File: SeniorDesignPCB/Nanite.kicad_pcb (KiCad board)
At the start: 2 copper layers, 20 parts, among them U1 4017, U2 TLC555

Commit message: Finished making lines?
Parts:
- moved D17 76.1 mm to (106.7, 81.3)
- moved D22 52.6 mm to (121.9, 82.5)
- moved D18 26.8 mm to (101.6, 71.1)
- moved D19 21.9 mm to (57.1, 87.6)
- moved D21 20.9 mm to (100.3, 91.4)
- moved BT1 7.73 mm to (118.1, 121.9)
- moved D20 3.59 mm to (77.5, 100.3)
- turned R2 to 90 degrees
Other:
- board outline added: 154.9 x 76.2 mm
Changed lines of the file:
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@@
   (general
     (thickness 1.6)
-    (drawings 0)
+    (drawings 5)
     (tracks 0)
     (zones 0)
@@
   )
   (module Battery:BatteryHolder_Keystone_2466_1xAAA (layer F.Cu)
-    (at 119.38 129.54)
+    (at 118.11 121.92)
     (descr "1xAAA Battery Holder, Keystone, Plastic Case, http://www.keyelco.com/product-pdf.cfm?p=1031")
     (tags "AAA battery holder Keystone")
@@
   )
   (module Diode_THT:D_DO-41_SOD81_P10.16mm_Horizontal (layer F.Cu)
-    (at 80.01 114.3)
+    (at 121.92 82.55)
     (descr "Diode, DO-41_SOD81 series, Axial, Horizontal, pin pitch=10.16mm, , length*diameter=5.2*2.7mm^2, , http://www.diodes.com/_files/packages/DO-41%20(Plastic).pdf")
     (tags "Diode DO-41_SOD81 series Axial Horizontal pin pitch 10.16mm  length 5.2mm diameter 2.7mm")
@@
   )
   (module Diode_THT:D_DO-41_SOD81_P10.16mm_Horizontal (layer F.Cu)
-    (at 80.01 96.52)
+    (at 100.33 91.44)
     (descr "Diode, DO-41_SOD81 series, Axial, Horizontal, pin pitch=10.16mm, , length*diameter=5.2*2.7mm^2, , http://www.diodes.com/_files/packages/DO-41%20(Plastic).pdf")
     (tags "Diode DO-41_SOD81 series Axial Horizontal pin pitch 10.16mm  length 5.2mm diameter 2.7mm")
@@
   )
   (module Diode_THT:D_DO-41_SOD81_P10.16mm_Horizontal (layer F.Cu)
-    (at 80.01 102.87)
+    (at 77.47 100.33)
     (descr "Diode, DO-41_SOD81 series, Axial, Horizontal, pin pitch=10.16mm, , length*diameter=5.2*2.7mm^2, , http://www.diodes.com/_files/packages/DO-41%20(Plastic).pdf")
     (tags "Diode DO-41_SOD81 series Axial Horizontal pin pitch 10.16mm  length 5.2mm diameter 2.7mm")
@@
   )
   (module Diode_THT:D_DO-41_SOD81_P10.16mm_Horizontal (layer F.Cu)
-    (at 78.74 91.44)
+    (at 57.15 87.63)
     (descr "Diode, DO-41_SOD81 series, Axial, Horizontal, pin pitch=10.16mm, , length*diameter=5.2*2.7mm^2, , http://www.diodes.com/_files/packages/DO-41%20(Plastic).pdf")
     (tags "Diode DO-41_SOD81 series Axial Horizontal pin pitch 10.16mm  length 5.2mm diameter 2.7mm")
@@
   )
   (module Diode_THT:D_DO-41_SOD81_P10.16mm_Horizontal (layer F.Cu)
-    (at 78.74 85.09)
+    (at 101.6 71.12)
     (descr "Diode, DO-41_SOD81 series, Axial, Horizontal, pin pitch=10.16mm, , length*diameter=5.2*2.7mm^2, , http://www.diodes.com/_files/packages/DO-41%20(Plastic).pdf")
     (tags "Diode DO-41_SOD81 series Axial Horizontal pin pitch 10.16mm  length 5.2mm diameter 2.7mm")
@@
   )
   (module LED_THT:LED_D5.0mm (layer F.Cu)
-    (at 43.18 123.19)
+    (at 106.68 81.28)
     (descr "LED, diameter 5.0mm, 2 pins, http://cdn-reichelt.de/documents/datenblatt/A500/LL-504BC2E-009.pdf")
     (tags "LED diameter 5.0mm 2 pins")
@@
   )
   (module Resistor_THT:R_Axial_DIN0309_L9.0mm_D3.2mm_P2.54mm_Vertical (layer F.Cu)
-    (at 91.44 132.08)
+    (at 91.44 132.08 90)
     (descr "Resistor, Axial_DIN0309 series, Axial, Vertical, pin pitch=2.54mm, 0.5W = 1/2W, length*diameter=9*3.2mm^2, http://cdn-reichelt.de/documents/datenblatt/B400/1_4W%23YAG.pdf")
     (tags "Resistor Axial_DIN0309 series Axial Vertical pin pitch 2.54mm 0.5W = 1/2W length 9mm diameter 3.2mm")
-    (fp_text reference R2 (at 1.27 -2.72) (layer F.SilkS)
-      (effects (font (size 1 1) (thickness 0.15)))
-    )
-    (fp_text value 4.7k (at 1.27 2.72) (layer F.Fab)
+    (fp_text reference R2 (at 1.27 -2.72 90) (layer F.SilkS)
+      (effects (font (size 1 1) (thickness 0.15)))
+    )
+    (fp_text value 4.7k (at 1.27 2.72 90) (layer F.Fab)
       (effects (font (size 1 1) (thickness 0.15)))
     )
@@
     (fp_line (start 3.59 1.85) (end 3.59 -1.85) (layer F.CrtYd) (width 0.05))
     (fp_line (start 3.59 -1.85) (end -1.85 -1.85) (layer F.CrtYd) (width 0.05))
-    (fp_text user %R (at 1.27 -2.72) (layer F.Fab)
-      (effects (font (size 1 1) (thickness 0.15)))
-    )
-    (pad 1 thru_hole circle (at 0 0) (size 1.6 1.6) (drill 0.8) (layers *.Cu *.Mask)
+    (fp_text user %R (at 1.27 -2.72 90) (layer F.Fab)
+      (effects (font (size 1 1) (thickness 0.15)))
+    )
+    (pad 1 thru_hole circle (at 0 0 90) (size 1.6 1.6) (drill 0.8) (layers *.Cu *.Mask)
       (net 1 "Net-(BT1-Pad1)"))
-    (pad 2 thru_hole oval (at 2.54 0) (size 1.6 1.6) (drill 0.8) (layers *.Cu *.Mask)
+    (pad 2 thru_hole oval (at 2.54 0 90) (size 1.6 1.6) (drill 0.8) (layers *.Cu *.Mask)
       (net 2 "Net-(R2-Pad2)"))
     (model ${KISYS3DMOD}/Resistor_THT.3dshapes/R_Axial_DIN0309_L9.0mm_D3.2mm_P2.54mm_Vertical.wrl
@@
     )
   )
+  (gr_line (start 177.8 134.62) (end 177.8 138.43) (layer Edge.Cuts) (width 0.15))
+  (gr_line (start 177.8 62.23) (end 177.8 134.62) (layer Edge.Cuts) (width 0.15))
+  (gr_line (start 22.86 62.23) (end 177.8 62.23) (layer Edge.Cuts) (width 0.15))
+  (gr_line (start 22.86 138.43) (end 177.8 138.43) (layer Edge.Cuts) (width 0.15))
+  (gr_line (start 22.86 62.23) (end 22.86 138.43) (layer Edge.Cuts) (width 0.15))
 )

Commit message: Added all tracings
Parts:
- U1: footprint Johnson Counter 4017:DecadeCounter -> 74HC4017D_653:SOIC127P600X175-16N
- U2: value TLC555 -> 555TIMER; footprint 555 Timer:TLC555 -> LM555CN_Timer:DIP762W53P254L980H533Q8N
- moved R1 102.2 mm to (127.0, 77.5), turned to 0 degrees
- moved D19 78.2 mm to (133.3, 69.8), turned to 180 degrees
- moved D14 64.3 mm to (92.7, 72.4)
- moved D13 54.6 mm to (92.7, 115.6)
- moved D15 52.6 mm to (92.7, 92.7)
- moved D20 50.9 mm to (128.3, 104.1), turned to 180 degrees
- moved D12 49.6 mm to (92.7, 82.5)
- moved D16 49.6 mm to (92.7, 104.1)
- moved D17 46.6 mm to (92.7, 125.7)
- moved C2 38.4 mm to (129.5, 111.8)
- moved R2 36.6 mm to (121.9, 111.8), turned to 0 degrees
- moved R3 28.7 mm to (127.0, 86.4), turned to 180 degrees
- moved C1 23.2 mm to (147.3, 108.0), turned to 0 degrees
- moved D18 11.4 mm to (101.6, 82.5)
- moved RV1 10.9 mm to (153.7, 90.2), turned to 90 degrees
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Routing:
- net GNDA: track 0.00 -> 186.4 mm
- net Net-(D12-Pad1): track 0.00 -> 103.2 mm
- net Net-(D13-Pad2): track 0.00 -> 90.8 mm, vias 0 -> 1
- net Net-(D14-Pad2): track 0.00 -> 86.9 mm, vias 0 -> 1
- net Net-(D17-Pad2): track 0.00 -> 55.8 mm
- net Net-(D15-Pad2): track 0.00 -> 53.3 mm
- net Net-(R2-Pad2): track 0.00 -> 45.4 mm
- net Net-(R3-Pad1): track 0.00 -> 28.2 mm
- net Net-(D19-Pad2): track 0.00 -> 27.8 mm, vias 0 -> 2
- net Net-(D16-Pad2): track 0.00 -> 26.6 mm
- net Net-(D22-Pad2): track 0.00 -> 23.9 mm
- net Net-(U1-Pad14): track 0.00 -> 18.7 mm, vias 0 -> 1
- net Net-(RV1-Pad2): track 0.00 -> 17.3 mm
- net Net-(C2-Pad1): track 0.00 -> 15.5 mm, vias 0 -> 1
- net Net-(D18-Pad2): track 0.00 -> 14.1 mm
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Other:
- board outline removed

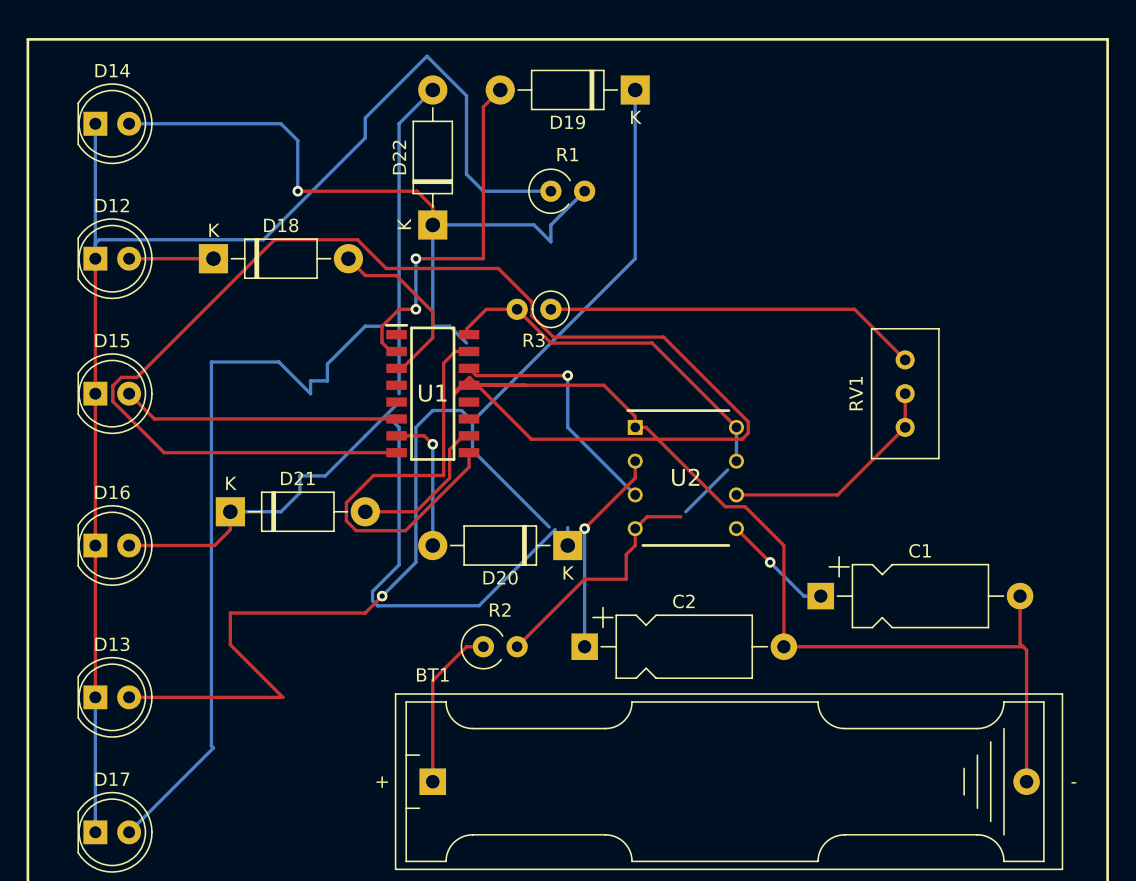
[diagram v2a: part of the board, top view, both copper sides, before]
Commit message: one last connection new diode
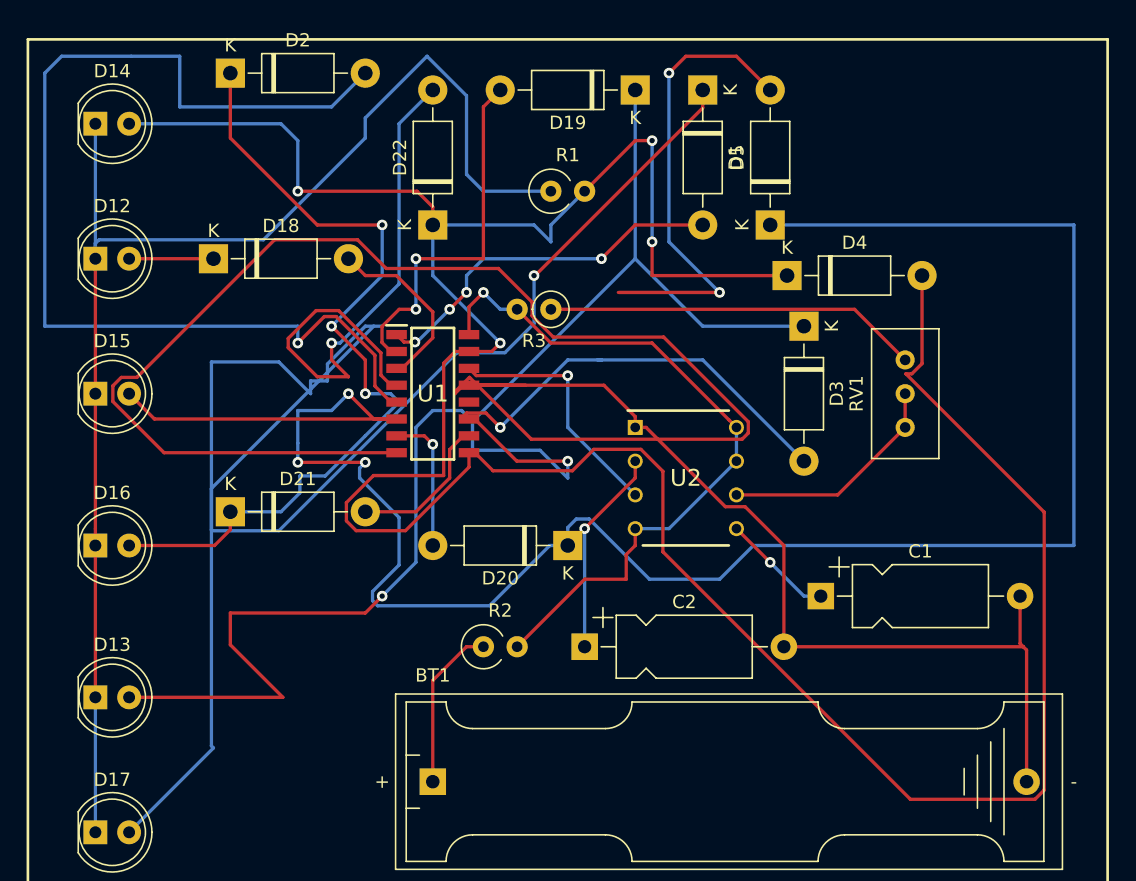
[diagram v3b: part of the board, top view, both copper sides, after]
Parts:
- added D1: 1N4007, Diode_THT:D_DO-41_SOD81_P10.16mm_Horizontal, F.Cu at (138.4, 69.8)
- added D2: 1N4007, Diode_THT:D_DO-41_SOD81_P10.16mm_Horizontal, F.Cu at (102.9, 68.6)
- added D3: 1N4007, Diode_THT:D_DO-41_SOD81_P10.16mm_Horizontal, F.Cu at (146.1, 87.6)
- added D4: 1N4007, Diode_THT:D_DO-41_SOD81_P10.16mm_Horizontal, F.Cu at (144.8, 83.8)
- added D5: 1N4007, Diode_THT:D_DO-41_SOD81_P10.16mm_Horizontal, F.Cu at (143.5, 80.0)
- U2: value 555TIMER -> TLC555
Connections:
- D17 pad 2: Net-(D17-Pad2) -> Net-(D1-Pad1)
- U1 pad 1: Net-(D17-Pad2) -> Net-(D1-Pad2)
- U1 pad 11: Net-(D13-Pad2) -> Net-(D3-Pad2)
- U1 pad 5: Net-(D16-Pad2) -> Net-(D2-Pad2)
- U1 pad 6: Net-(D15-Pad2) -> Net-(D5-Pad2)
- U1 pad 9: Net-(D14-Pad2) -> Net-(D4-Pad2)
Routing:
- net Net-(D1-Pad1): track 0.00 -> 129.4 mm, vias 0 -> 1
- net Net-(D15-Pad2): track 53.3 -> 157.7 mm, vias 0 -> 3
- net Net-(D4-Pad2): track 0.00 -> 102.6 mm
- net Net-(D2-Pad2): track 0.00 -> 81.2 mm, vias 0 -> 1
- net Net-(D17-Pad2): track 55.8 -> 0.00 mm
- net Net-(D16-Pad2): track 26.6 -> 63.7 mm, vias 0 -> 3
- net Net-(D5-Pad2): track 0.00 -> 34.9 mm, vias 0 -> 2
- net Net-(D3-Pad2): track 0.00 -> 32.1 mm, vias 0 -> 1
- net Net-(D14-Pad2): track 86.9 -> 116.8 mm, vias 1 -> 4
- net Net-(D1-Pad2): track 0.00 -> 28.1 mm, vias 0 -> 4
- net Net-(D13-Pad2): track 90.8 -> 115.5 mm, vias 1 -> 2
- net Net-(D22-Pad2): track 23.9 -> 44.1 mm, vias 0 -> 1
- net Net-(R2-Pad2): track 45.4 -> 53.6 mm, vias 0 -> 1
- net (no net): track 4.46 -> 0.00 mm

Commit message: Fixing errors with DRC, done tracing
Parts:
- moved D5 53.6 mm to (111.8, 123.2), turned to 180 degrees
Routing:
- net Net-(D15-Pad2): track 157.7 -> 126.3 mm
- net Net-(D5-Pad2): track 34.9 -> 49.1 mm, vias 2 -> 3
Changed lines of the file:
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@@
     (thickness 1.6)
     (drawings 4)
-    (tracks 330)
+    (tracks 335)
     (zones 0)
     (modules 25)
@@
   )
   (module Diode_THT:D_DO-41_SOD81_P10.16mm_Horizontal (layer F.Cu)
-    (at 143.51 80.01 90)
+    (at 111.76 123.19 180)
     (descr "Diode, DO-41_SOD81 series, Axial, Horizontal, pin pitch=10.16mm, , length*diameter=5.2*2.7mm^2, , http://www.diodes.com/_files/packages/DO-41%20(Plastic).pdf")
     (tags "Diode DO-41_SOD81 series Axial Horizontal pin pitch 10.16mm  length 5.2mm diameter 2.7mm")
-    (fp_text reference D5 (at 5.08 -2.47 90) (layer F.SilkS)
-      (effects (font (size 1 1) (thickness 0.15)))
-    )
-    (fp_text value 1N4007 (at 5.08 2.47 90) (layer F.Fab)
+    (fp_text reference D5 (at 5.08 -2.47 180) (layer F.SilkS)
+      (effects (font (size 1 1) (thickness 0.15)))
+    )
+    (fp_text value 1N4007 (at 5.08 2.47 180) (layer F.Fab)
       (effects (font (size 1 1) (thickness 0.15)))
     )
@@
     (fp_line (start 11.51 1.6) (end 11.51 -1.6) (layer F.CrtYd) (width 0.05))
     (fp_line (start 11.51 -1.6) (end -1.35 -1.6) (layer F.CrtYd) (width 0.05))
-    (fp_text user %R (at 5.47 0 90) (layer F.Fab)
-      (effects (font (size 1 1) (thickness 0.15)))
-    )
-    (fp_text user K (at 0 -2.1 90) (layer F.Fab)
-      (effects (font (size 1 1) (thickness 0.15)))
-    )
-    (fp_text user K (at 0 -2.1 90) (layer F.SilkS)
-      (effects (font (size 1 1) (thickness 0.15)))
-    )
-    (pad 1 thru_hole rect (at 0 0 90) (size 2.2 2.2) (drill 1.1) (layers *.Cu *.Mask)
+    (fp_text user %R (at 5.47 0 180) (layer F.Fab)
+      (effects (font (size 1 1) (thickness 0.15)))
+    )
+    (fp_text user K (at 0 -2.1 180) (layer F.Fab)
+      (effects (font (size 1 1) (thickness 0.15)))
+    )
+    (fp_text user K (at 0 -2.1 180) (layer F.SilkS)
+      (effects (font (size 1 1) (thickness 0.15)))
+    )
+    (pad 1 thru_hole rect (at 0 0 180) (size 2.2 2.2) (drill 1.1) (layers *.Cu *.Mask)
       (net 8 "Net-(D15-Pad2)"))
-    (pad 2 thru_hole oval (at 10.16 0 90) (size 2.2 2.2) (drill 1.1) (layers *.Cu *.Mask)
+    (pad 2 thru_hole oval (at 10.16 0 180) (size 2.2 2.2) (drill 1.1) (layers *.Cu *.Mask)
       (net 24 "Net-(D5-Pad2)"))
     (model ${KISYS3DMOD}/Diode_THT.3dshapes/D_DO-41_SOD81_P10.16mm_Horizontal.wrl
@@
   (segment (start 128.915001 102.144999) (end 128.27 102.79) (width 0.25) (layer B.Cu) (net 8))
   (segment (start 129.888001 102.144999) (end 128.915001 102.144999) (width 0.25) (layer B.Cu) (net 8))
-  (segment (start 143.51 80.01) (end 166.37 80.01) (width 0.25) (layer B.Cu) (net 8))
   (segment (start 166.37 104.14) (end 142.24 104.14) (width 0.25) (layer B.Cu) (net 8))
   (segment (start 142.24 104.14) (end 139.7 106.68) (width 0.25) (layer B.Cu) (net 8))
-  (segment (start 166.37 80.01) (end 166.37 104.14) (width 0.25) (layer B.Cu) (net 8))
   (segment (start 139.7 106.68) (end 134.423002 106.68) (width 0.25) (layer B.Cu) (net 8))
   (segment (start 134.423002 106.68) (end 129.888001 102.144999) (width 0.25) (layer B.Cu) (net 8))
+  (segment (start 111.76 110.113) (end 113.574999 108.298001) (width 0.25) (layer B.Cu) (net 8))
+  (segment (start 111.76 123.19) (end 111.76 110.113) (width 0.25) (layer B.Cu) (net 8))
   (segment (start 95.25 115.57) (end 106.824999 115.57) (width 0.25) (layer F.Cu) (net 9))
   (segment (start 102.87 111.615001) (end 102.87 109.22) (width 0.25) (layer F.Cu) (net 9))
@@
   (segment (start 115.944847 88.824847) (end 115.385 88.265) (width 0.25) (layer F.Cu) (net 23))
   (segment (start 116.764847 88.824847) (end 115.944847 88.824847) (width 0.25) (layer F.Cu) (net 23))
-  (segment (start 143.51 69.85) (end 140.97 67.31) (width 0.25) (layer F.Cu) (net 24))
-  (via (at 135.89 68.58) (size 0.8) (drill 0.4) (layers F.Cu B.Cu) (net 24))
-  (segment (start 140.97 67.31) (end 137.16 67.31) (width 0.25) (layer F.Cu) (net 24))
-  (segment (start 137.16 67.31) (end 135.89 68.58) (width 0.25) (layer F.Cu) (net 24))
-  (via (at 139.7 85.09) (size 0.8) (drill 0.4) (layers F.Cu B.Cu) (net 24))
-  (segment (start 135.89 68.58) (end 135.89 81.28) (width 0.25) (layer B.Cu) (net 24))
-  (segment (start 135.89 81.28) (end 139.7 85.09) (width 0.25) (layer B.Cu) (net 24))
-  (segment (start 139.7 85.09) (end 132.08 85.09) (width 0.25) (layer F.Cu) (net 24))
+  (segment (start 102.87 121.92) (end 102.87 110.49) (width 0.25) (layer B.Cu) (net 24))
+  (segment (start 101.6 123.19) (end 102.87 121.92) (width 0.25) (layer B.Cu) (net 24))
+  (via (at 102.87 106.68) (size 0.8) (drill 0.4) (layers F.Cu B.Cu) (net 24))
+  (segment (start 102.87 110.49) (end 102.87 106.68) (width 0.25) (layer B.Cu) (net 24))
+  (via (at 99.06 106.68) (size 0.8) (drill 0.4) (layers F.Cu B.Cu) (net 24))
+  (segment (start 102.87 106.68) (end 99.06 106.68) (width 0.25) (layer F.Cu) (net 24))
+  (via (at 99.06 96.43) (size 0.8) (drill 0.4) (layers F.Cu B.Cu) (net 24))
+  (segment (start 99.06 106.68) (end 99.06 96.43) (width 0.25) (layer B.Cu) (net 24))
+  (segment (start 115.83501 94.4286) (end 115.703205 94.296795) (width 0.25) (layer F.Cu) (net 24))
+  (segment (start 115.83501 94.8014) (end 115.83501 94.4286) (width 0.25) (layer F.Cu) (net 24))
+  (segment (start 115.5714 95.06501) (end 115.83501 94.8014) (width 0.25) (layer F.Cu) (net 24))
+  (segment (start 100.42499 95.06501) (end 115.5714 95.06501) (width 0.25) (layer F.Cu) (net 24))
+  (segment (start 99.06 96.43) (end 100.42499 95.06501) (width 0.25) (layer F.Cu) (net 24))
   (segment (start 146.05 97.79) (end 138.43 90.17) (width 0.25) (layer B.Cu) (net 25))
   (via (at 123.19 95.25) (size 0.8) (drill 0.4) (layers F.Cu B.Cu) (net 25))
